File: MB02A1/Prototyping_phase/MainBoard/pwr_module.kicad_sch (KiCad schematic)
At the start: 15 parts, among them J4 USB_B_Mini, Q1 BC369, Q2 BC369

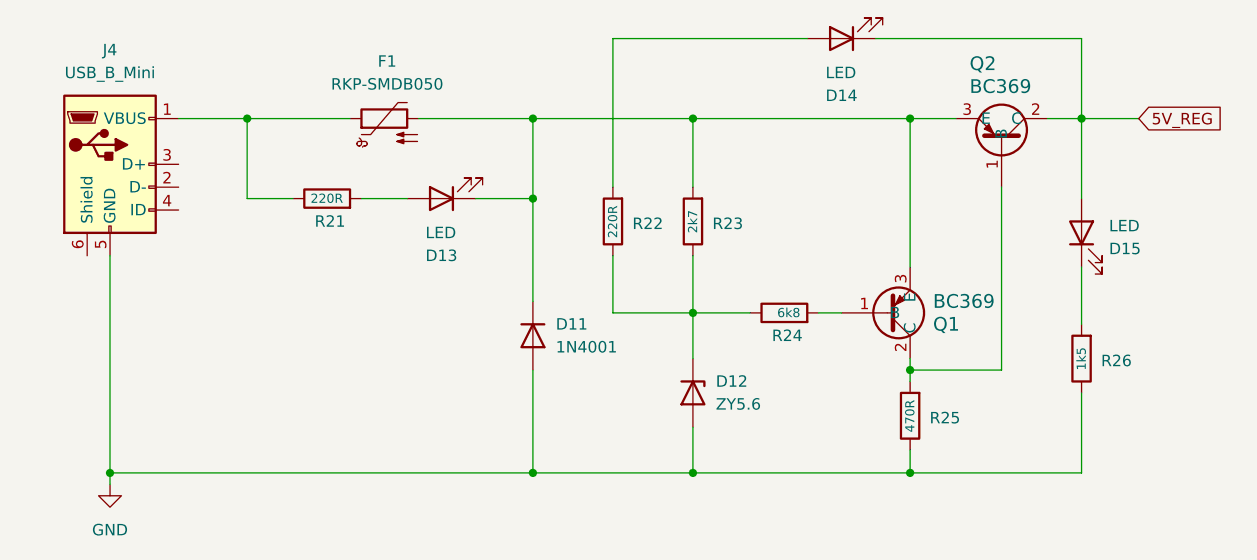
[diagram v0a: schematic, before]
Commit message: Datasheets added, design updated.
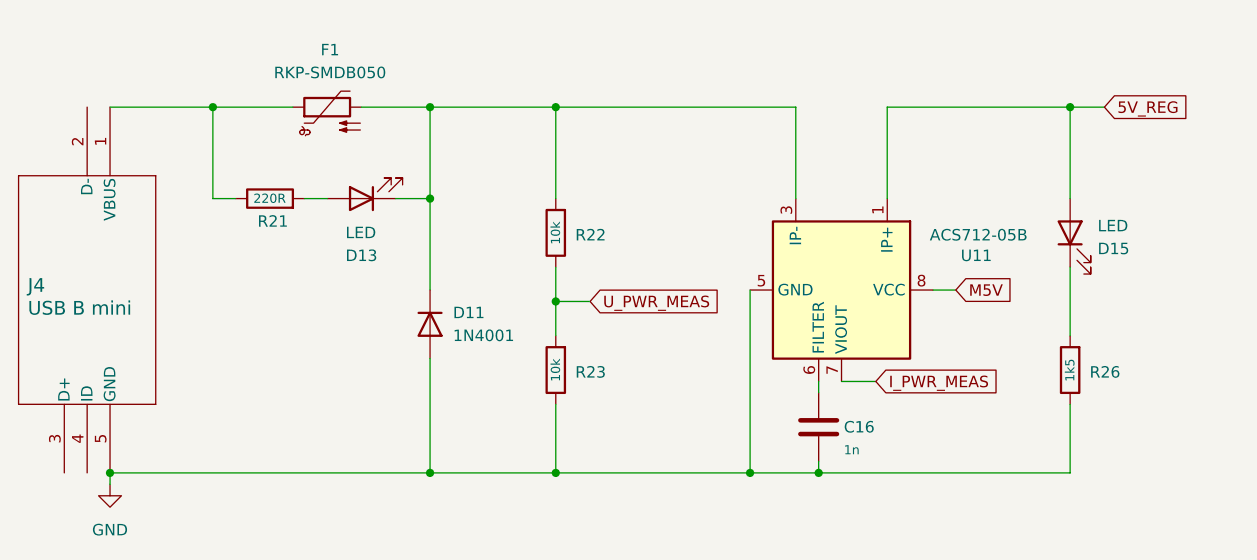
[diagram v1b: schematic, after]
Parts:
- removed D12: ZY5.6, Diode_THT:D_DO-41_SOD81_P10.16mm_Horizontal, symbol Diode:ZYxxx
- removed D14: LED, LED_SMD:LED_1206_3216Metric, symbol Device:LED
- removed J4: USB_B_Mini, Connector_USB:USB_Mini-B_Wuerth_65100516121_Horizontal, symbol Connector:USB_B_Mini
- removed Q1, Q2: BC369, footprints:TO-92_ONS, symbol 2025-01-17_22-35-13:BC369
- removed R24: 6k8, Resistor_SMD:R_0805_2012Metric, symbol Device:R
- removed R25: 470R, Resistor_SMD:R_0805_2012Metric, symbol Device:R
- added C16: 1n, Capacitor_SMD:C_0805_2012Metric, symbol Device:C
- added J4: USB B mini, 54819-0519_MOL, symbol USB_B_mini_th:548190519
- added U11: ACS712-05B, Package_SO:SOIC-8_3.9x4.9mm_P1.27mm, symbol Sensor_Current:ACS712xLCTR-05B
- R22: value 220R -> 10k
- R23: value 2k7 -> 10k
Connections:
- net 5V_REG: now also U11.1 (IP+), U11.2 (IP+)
- net GND: now also R23.1, C16.2, J4.5 (GND), U11.5 (GND)
- net at D11.1 (K), D13.1 (K), F1.2: now also R22.2, U11.3 (IP-), U11.4 (IP-); no longer R23.2
- net at F1.1, R21.1: now also J4.1 (VBUS)
- net U_PWR_MEAS: now reaches R22.1
- net U_PWR_MEAS: now also R23.2; no longer R23.1
- new net: C16.1, U11.6 (FILTER)
- new net I_PWR_MEAS: U11.7 (VIOUT)
- new net M5V: U11.8 (VCC)
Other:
- moved on the sheet: D11, D13, D15, F1, R21, R26

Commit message: Design update, production preparation.
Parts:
- renumbered C16 to C1, D13 to D1, D11 to D2, D15 to D3, J4 to J1, R21 to R1, R22 to R2, R23 to R3, R26 to R4, U11 to U1
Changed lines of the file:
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@@
 	(wire
 		(pts
-			(xy 179.07 109.22) (xy 182.88 109.22)
+			(xy 179.07 109.22) (xy 184.15 109.22)
 		)
 		(stroke
@@
 	(global_label "I_PWR_MEAS"
 		(shape input)
-		(at 182.88 109.22 0)
+		(at 184.15 109.22 0)
 		(fields_autoplaced yes)
 		(effects
@@
 		)
 		(property "Intersheetrefs" "${INTERSHEET_REFS}"
-			(at 197.2951 109.22 0)
+			(at 198.5651 109.22 0)
 			(effects
 				(font
@@
 		(on_board yes)
 		(dnp no)
-		(property "Reference" "D13"
+		(property "Reference" "D1"
 			(at 123.952 95.25 0)
 			(effects
@@
 			(project "mb02a1"
 				(path "/ee4e0941-1c36-4545-8b22-b979d73b3a97/c17459ea-fd75-4a33-b501-4f0ee6f3a833"
-					(reference "D13")
+					(reference "D1")
 					(unit 1)
 				)
@@
 		(on_board yes)
 		(dnp no)
-		(property "Reference" "R21"
+		(property "Reference" "R1"
 			(at 117.602 91.44 90)
 			(effects
@@
 			(project "mb02a1"
 				(path "/ee4e0941-1c36-4545-8b22-b979d73b3a97/c17459ea-fd75-4a33-b501-4f0ee6f3a833"
-					(reference "R21")
+					(reference "R1")
 					(unit 1)
 				)
@@
 		(on_board yes)
 		(dnp no)
-		(property "Reference" "R23"
+		(property "Reference" "R3"
 			(at 152.908 108.204 0)
 			(effects
@@
 			(project "mb02a1"
 				(path "/ee4e0941-1c36-4545-8b22-b979d73b3a97/c17459ea-fd75-4a33-b501-4f0ee6f3a833"
-					(reference "R23")
+					(reference "R3")
 					(unit 1)
 				)
@@
 		(dnp no)
 		(fields_autoplaced yes)
-		(property "Reference" "#PWR028"
+		(property "Reference" "#PWR01"
 			(at 97.79 127 0)
 			(effects
@@
 			(project "mb02a1"
 				(path "/ee4e0941-1c36-4545-8b22-b979d73b3a97/c17459ea-fd75-4a33-b501-4f0ee6f3a833"
-					(reference "#PWR028")
+					(reference "#PWR01")
 					(unit 1)
 				)
@@
 		(on_board yes)
 		(dnp no)
-		(property "Reference" "R22"
+		(property "Reference" "R2"
 			(at 152.908 92.964 0)
 			(effects
@@
 			(project "mb02a1"
 				(path "/ee4e0941-1c36-4545-8b22-b979d73b3a97/c17459ea-fd75-4a33-b501-4f0ee6f3a833"
-					(reference "R22")
+					(reference "R2")
 					(unit 1)
 				)
@@
 		(on_board yes)
 		(dnp no)
-		(property "Reference" "R26"
+		(property "Reference" "R4"
 			(at 210.058 108.204 0)
 			(effects
@@
 			(project "mb02a1"
 				(path "/ee4e0941-1c36-4545-8b22-b979d73b3a97/c17459ea-fd75-4a33-b501-4f0ee6f3a833"
-					(reference "R26")
+					(reference "R4")
 					(unit 1)
 				)
@@
 		(on_board yes)
 		(dnp no)
-		(property "Reference" "C16"
+		(property "Reference" "C1"
 			(at 179.324 114.3 0)
 			(effects
@@
 			(project "mb02a1"
 				(path "/ee4e0941-1c36-4545-8b22-b979d73b3a97/c17459ea-fd75-4a33-b501-4f0ee6f3a833"
-					(reference "C16")
+					(reference "C1")
 					(unit 1)
 				)
@@
 		(on_board yes)
 		(dnp no)
-		(property "Reference" "D15"
+		(property "Reference" "D3"
 			(at 207.518 94.488 90)
 			(effects
@@
 			(project "mb02a1"
 				(path "/ee4e0941-1c36-4545-8b22-b979d73b3a97/c17459ea-fd75-4a33-b501-4f0ee6f3a833"
-					(reference "D15")
+					(reference "D3")
 					(unit 1)
 				)
@@
 		(on_board yes)
 		(dnp no)
-		(property "Reference" "U11"
+		(property "Reference" "U1"
 			(at 194.056 95.25 90)
 			(effects
@@
 			(project ""
 				(path "/ee4e0941-1c36-4545-8b22-b979d73b3a97/c17459ea-fd75-4a33-b501-4f0ee6f3a833"
-					(reference "U11")
+					(reference "U1")
 					(unit 1)
 				)
@@
 		(on_board yes)
 		(dnp no)
-		(property "Reference" "J4"
+		(property "Reference" "J1"
 			(at 88.646 98.552 90)
 			(effects
@@
 			(project "mb02a1"
 				(path "/ee4e0941-1c36-4545-8b22-b979d73b3a97/c17459ea-fd75-4a33-b501-4f0ee6f3a833"
-					(reference "J4")
+					(reference "J1")
 					(unit 1)
 				)
@@
 		(dnp no)
 		(fields_autoplaced yes)
-		(property "Reference" "D11"
+		(property "Reference" "D2"
 			(at 135.89 101.5999 90)
 			(effects
@@
 			(project ""
 				(path "/ee4e0941-1c36-4545-8b22-b979d73b3a97/c17459ea-fd75-4a33-b501-4f0ee6f3a833"
-					(reference "D11")
+					(reference "D2")
 					(unit 1)
 				)
